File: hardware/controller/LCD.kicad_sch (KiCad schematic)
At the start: 1 part, among them U2 3.2inch_IPS_SPI_Module_ILI9341

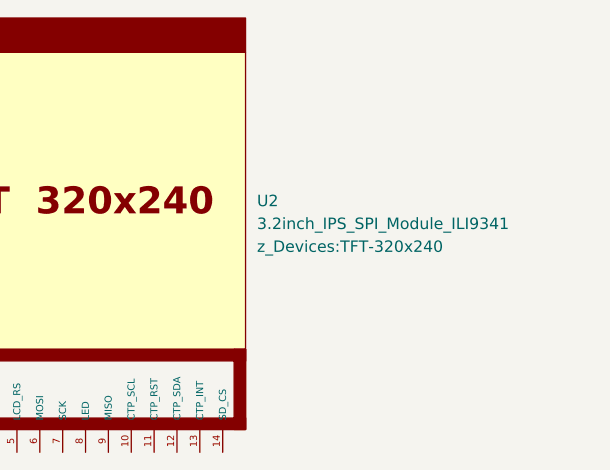
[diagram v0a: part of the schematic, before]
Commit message: added LED IC's and USB UART bridge
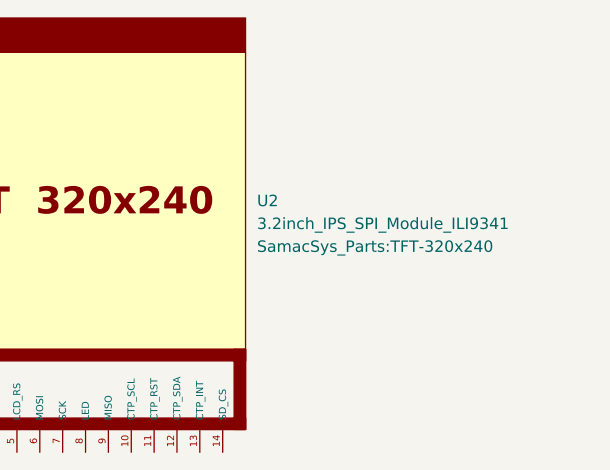
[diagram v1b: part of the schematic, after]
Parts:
- U2: footprint z_Devices:TFT-320x240 -> SamacSys_Parts:TFT-320x240
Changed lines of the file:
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@@
 			)
 		)
-		(property "Footprint" "z_Devices:TFT-320x240"
+		(property "Footprint" "SamacSys_Parts:TFT-320x240"
 			(at 157.48 74.9299 0)
 			(effects

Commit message: asdasd
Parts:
- renumbered U2 to U1
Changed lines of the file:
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@@
 		(dnp no)
 		(fields_autoplaced yes)
-		(property "Reference" "U2"
+		(property "Reference" "U1"
 			(at 157.48 69.8499 0)
 			(effects
@@
 			(project ""
 				(path "/869bea87-c885-4ead-826b-3f34ceacafad/a91903fe-ee0b-42c2-9d54-da8a7ff8ed7e"
-					(reference "U2")
+					(reference "U1")
 					(unit 1)
 				)

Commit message: a
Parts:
- U1: footprint SamacSys_Parts:TFT-320x240 -> z_Devices:TFT-320x240
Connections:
- net +3V3: now reaches U1.1 (VCC)
- net CTP_SCL: now reaches U1.10 (CTP_SCL)
- net CTP_RST: now reaches U1.11 (~{CTP_RST})
- net CTP_SDA: now reaches U1.12 (CTP_SDA)
- net CTP_INT: now reaches U1.13 (~{CTP_INT})
- net SD_CS: now reaches U1.14 (~{SD_CS})
- net GND: now reaches U1.2 (GND)
- net LCD_CS: now reaches U1.3 (~{LCD_CS})
- net LCD_RST: now reaches U1.4 (~{LCD_RST})
- net LCD_RS: now reaches U1.5 (LCD_RS)
- net MOSI: now reaches U1.6 (MOSI)
- net SCK: now reaches U1.7 (SCK)
- net MISO: now reaches U1.9 (MISO)
- no-connect marks 0 -> 1

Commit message: fixed bus stuff
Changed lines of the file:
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@@
 	(generator_version "9.0")
 	(paper "A4")
+	(bus_alias "I2C_CTP_LED"
+		(members)
+	)
+	(bus_alias "SPI_LCD_SD"
+		(members "LCD_RST" "SCK" "MOSI" "SD_CS" "MISO" "LCD_CS")
+	)
 	(no_connect
 		(at 138.43 97.79)
@@
 		)
 	)
-	(hierarchical_label "I2C_LCD"
+	(hierarchical_label "I2C_CTP_LED{I2C_CTP_LED}"
 		(shape bidirectional)
 		(at 186.69 134.62 0)
@@
 		)
 	)
-	(hierarchical_label "SPI_LCD"
+	(hierarchical_label "SPI_LCD_SD{SPI_LCD_SD}"
 		(shape bidirectional)
 		(at 186.69 106.68 0)
@@
 		(dnp no)
 		(fields_autoplaced yes)
-		(property "Reference" "#PWR038"
+		(property "Reference" "#PWR015"
 			(at 123.19 104.14 0)
 			(effects
@@
 			(project ""
 				(path "/869bea87-c885-4ead-826b-3f34ceacafad/a91903fe-ee0b-42c2-9d54-da8a7ff8ed7e"
-					(reference "#PWR038")
+					(reference "#PWR015")
 					(unit 1)
 				)
@@
 		(dnp no)
 		(fields_autoplaced yes)
-		(property "Reference" "#PWR039"
+		(property "Reference" "#PWR014"
 			(at 114.3 101.6 0)
 			(effects
@@
 			(project ""
 				(path "/869bea87-c885-4ead-826b-3f34ceacafad/a91903fe-ee0b-42c2-9d54-da8a7ff8ed7e"
-					(reference "#PWR039")
+					(reference "#PWR014")
 					(unit 1)
 				)

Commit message: added memory and fixed gpio pins
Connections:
- net CTP_SCL renamed SCL
- net CTP_SDA renamed SDA
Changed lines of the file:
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@@
 	(paper "A4")
 	(bus_alias "I2C_CTP_LED"
-		(members)
+		(members "CTP_RST" "SCL" "CTP_INT" "SDA" "~{OE}")
 	)
 	(bus_alias "SPI_LCD_SD"
@@
 		)
 	)
-	(label "CTP_SDA"
+	(label "SDA"
 		(at 123.19 129.54 180)
 		(effects
@@
 		)
 	)
-	(label "I2C_CTP_LED.CTP_SCL"
+	(label "I2C_CTP_LED.SCL"
 		(at 185.42 124.46 180)
 		(effects
@@
 		)
 	)
-	(label "CTP_SCL"
+	(label "SCL"
 		(at 123.19 124.46 180)
 		(effects
@@
 		)
 	)
-	(label "I2C_CTP_LED.CTP_SDA"
+	(label "I2C_CTP_LED.SDA"
 		(at 185.42 121.92 180)
 		(effects

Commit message: lol
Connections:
- net CTP_INT is gone; now on net I2C_CTP_LED.CTP_INT: U1.13 (~{CTP_INT})
- net CTP_RST is gone; now on net I2C_CTP_LED.CTP_RST: U1.11 (~{CTP_RST})
- net LCD_CS is gone; now on net SPI_LCD_CS.LCD_CS: U1.3 (~{LCD_CS})
- net LCD_RST is gone; now on net SPI_LCD_CS.LCD_RST: U1.4 (~{LCD_RST})
- net MISO is gone; now on net SPI_LCD_CS.MISO: U1.9 (MISO)
- net MOSI is gone; now on net SPI_LCD_CS.MOSI: U1.6 (MOSI)
- net SCK is gone; now on net SPI_LCD_CS.SCK: U1.7 (SCK)
- net SCL is gone; now on net I2C_CTP_LED.SCL: U1.10 (CTP_SCL)
- net SDA is gone; now on net I2C_CTP_LED.SDA: U1.12 (CTP_SDA)
- net SD_CS is gone; now on net SPI_LCD_CS.SD_CS: U1.14 (~{SD_CS})
- net LCD_RS renamed SPI_LCD_CS.LCD_RS
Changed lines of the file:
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@@
-		)
-	)
-	(label "SD_CS"
-		(at 123.19 134.62 180)
-		(effects
-			(font
-				(size 1.27 1.27)
-			)
-			(justify right bottom)
 		)
 	)
@@
 		)
 	)
-	(label "LCD_RST"
-		(at 123.19 109.22 180)
+	(label "SPI_LCD_CS.LCD_CS"
+		(at 123.19 106.68 180)
 		(effects
 			(font
@@
 		)
 	)
-	(label "LCD_CS"
-		(at 123.19 106.68 180)
-		(effects
-			(font
-				(size 1.27 1.27)
-			)
-			(justify right bottom)
-		)
-	)
 	(label "I2C_CTP_LED.CTP_INT"
 		(at 185.42 129.54 180)
@@
 		)
 	)
-	(label "SDA"
-		(at 123.19 129.54 180)
+	(label "I2C_CTP_LED.SCL"
+		(at 123.19 124.46 180)
+		(effects
+			(font
+				(size 1.27 1.27)
+			)
+			(justify right bottom)
+		)
+	)
+	(label "SPI_LCD_CS.LCD_RST"
+		(at 123.19 109.22 180)
 		(effects
 			(font
@@
 		)
 	)
-	(label "LCD_RS"
-		(at 123.19 111.76 180)
-		(effects
-			(font
-				(size 1.27 1.27)
-			)
-			(justify right bottom)
-		)
-	)
-	(label "CTP_RST"
-		(at 123.19 127 180)
-		(effects
-			(font
-				(size 1.27 1.27)
-			)
-			(justify right bottom)
-		)
-	)
-	(label "CTP_INT"
-		(at 123.19 132.08 180)
-		(effects
-			(font
-				(size 1.27 1.27)
-			)
-			(justify right bottom)
-		)
-	)
-	(label "MOSI"
-		(at 123.19 114.3 180)
-		(effects
-			(font
-				(size 1.27 1.27)
-			)
-			(justify right bottom)
-		)
-	)
-	(label "SCK"
-		(at 123.19 116.84 180)
-		(effects
-			(font
-				(size 1.27 1.27)
-			)
-			(justify right bottom)
-		)
-	)
-	(label "SCL"
-		(at 123.19 124.46 180)
+	(label "SPI_LCD_CS.SD_CS"
+		(at 123.19 134.62 180)
 		(effects
 			(font
@@
 		)
 	)
-	(label "MISO"
+	(label "SPI_LCD_CS.MISO"
 		(at 123.19 121.92 180)
+		(effects
+			(font
+				(size 1.27 1.27)
+			)
+			(justify right bottom)
+		)
+	)
+	(label "SPI_LCD_CS.MOSI"
+		(at 123.19 114.3 180)
+		(effects
+			(font
+				(size 1.27 1.27)
+			)
+			(justify right bottom)
+		)
+	)
+	(label "I2C_CTP_LED.CTP_INT"
+		(at 123.19 132.08 180)
 		(effects
 			(font
@@
 		(effects
 			(font
+				(size 1.27 1.27)
+			)
+			(justify right bottom)
+		)
+	)
+	(label "SPI_LCD_CS.LCD_RS"
+		(at 123.19 111.76 180)
+		(effects
+			(font
+				(size 1.27 1.27)
+			)
+			(justify right bottom)
+		)
+	)
+	(label "I2C_CTP_LED.SDA"
+		(at 123.19 129.54 180)
+		(effects
+			(font
+				(size 1.27 1.27)
+			)
+			(justify right bottom)
+		)
+	)
+	(label "SPI_LCD_CS.SCK"
+		(at 123.19 116.84 180)
+		(effects
+			(font
+				(size 1.27 1.27)
+			)
+			(justify right bottom)
+		)
+	)
+	(label "I2C_CTP_LED.CTP_RST"
+		(at 123.19 127 180)
+		(effects
+			(font

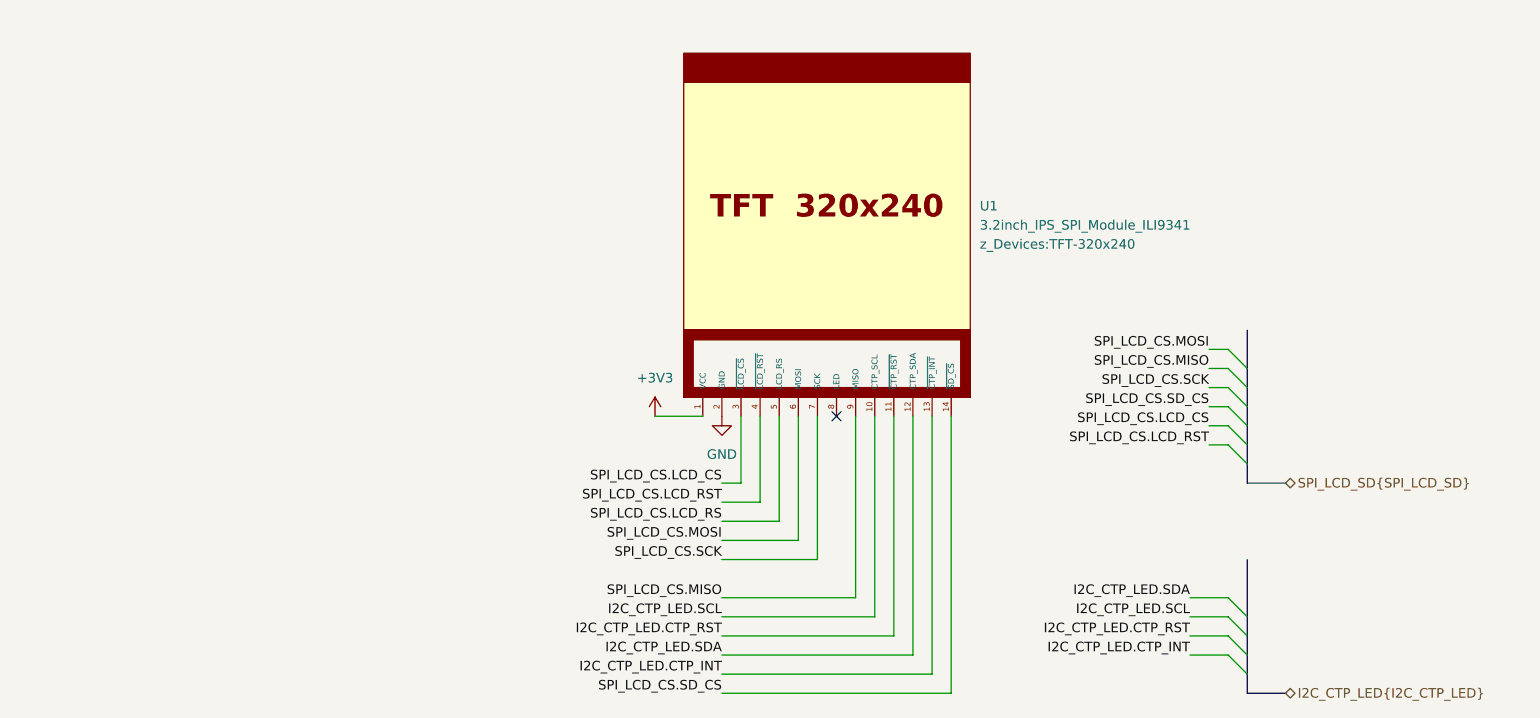
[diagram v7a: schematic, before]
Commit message: modified power circuitry
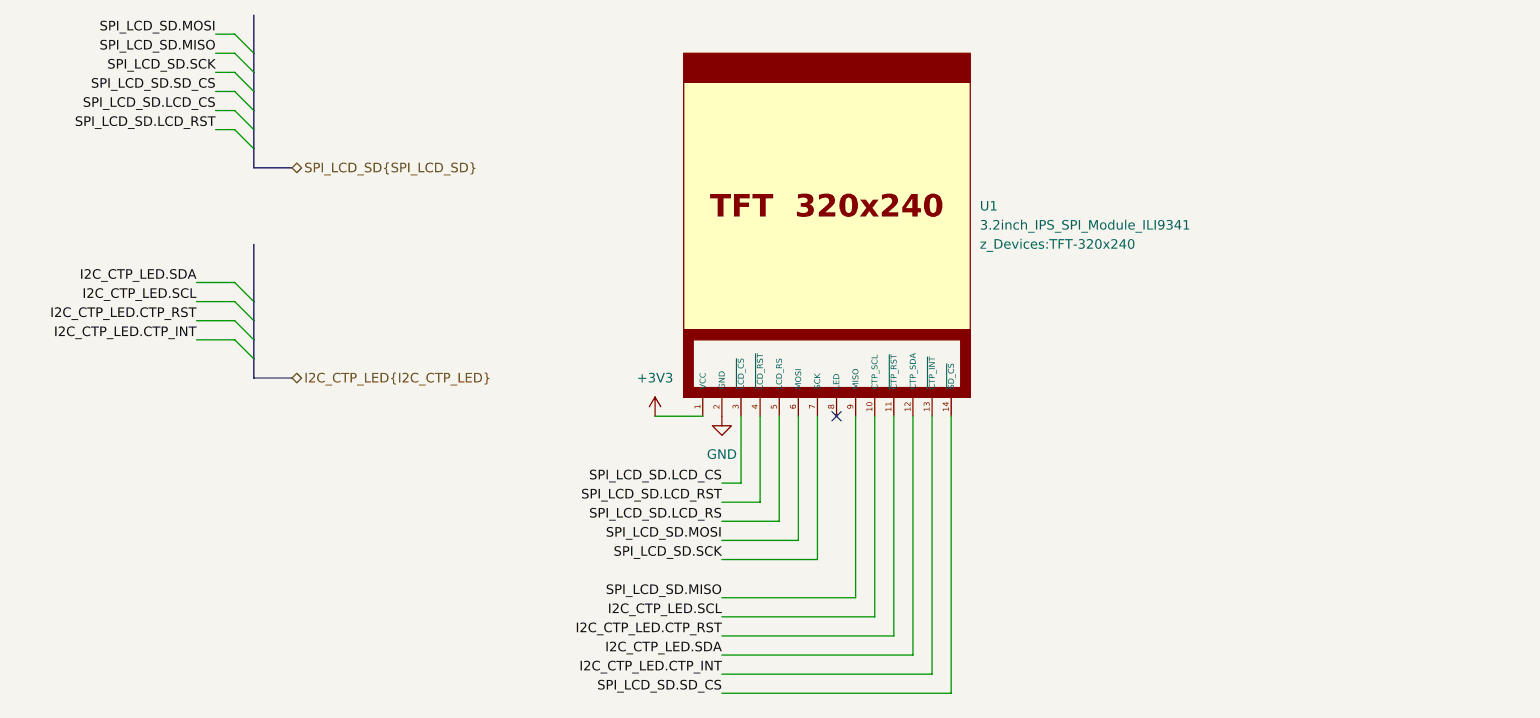
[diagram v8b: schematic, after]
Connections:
- net SPI_LCD_CS.LCD_CS renamed SPI_LCD_SD.LCD_CS
- net SPI_LCD_CS.LCD_RS renamed SPI_LCD_SD.LCD_RS
- net SPI_LCD_CS.LCD_RST renamed SPI_LCD_SD.LCD_RST
- net SPI_LCD_CS.MISO renamed SPI_LCD_SD.MISO
- net SPI_LCD_CS.MOSI renamed SPI_LCD_SD.MOSI
- net SPI_LCD_CS.SCK renamed SPI_LCD_SD.SCK
- net SPI_LCD_CS.SD_CS renamed SPI_LCD_SD.SD_CS
